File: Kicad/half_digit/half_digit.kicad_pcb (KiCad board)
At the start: 2 copper layers, 106.7 x 152.4 mm, 39 parts, among them J1 CONN_8, J2 CONN_8, J3 CONN_8, J4 CONN_8, J5 CONN_12, J6 CONN_12, J7 BARREL_JACK, U1 TLC5917, U2 AOZ1280, X1 MTHOLE, X2 MTHOLE, X3 MTHOLE, X4 MTHOLE

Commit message: Rough draft of half digit layout
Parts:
- added J8: CONN_12, HEADER_12X1, F.Cu at (135.3, 74.3)
- added J9: BARREL_JACK, PJ-036AH-SMT, F.Cu at (167.0, 205.7)
- J7: value BARREL_JACK -> CONN_12; footprint PJ-036AH-SMT -> HEADER_12X1
- moved J1 349.7 mm to (76.2, 205.7)
- moved J3 349.7 mm to (86.4, 205.7)
- moved R1 247.2 mm to (114.9, 130.2), turned to 90 degrees
- moved C4 236.8 mm to (119.4, 123.2), turned to 270 degrees
- moved C3 231.4 mm to (129.5, 195.6)
- moved D10 231.4 mm to (117.7, 144.8)
- moved D13 231.4 mm to (150.4, 144.8)
- moved D14 231.4 mm to (160.4, 144.8)
- moved D16 231.4 mm to (127.6, 200.0)
- moved D2 231.4 mm to (85.2, 113.9)
- moved D4 231.4 mm to (98.5, 190.8)
- moved D5 231.4 mm to (95.9, 176.0), turned to 180 degrees
- moved D6 231.4 mm to (93.3, 161.2)
- moved D7 231.4 mm to (137.3, 133.4), turned to 180 degrees
- moved D9 231.4 mm to (127.7, 144.8)
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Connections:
- J5 pad 12: (no net) -> N-0000031
- J5 pad 3: (no net) -> N-0000018
- J5 pad 4: (no net) -> N-0000017
- J5 pad 5: (no net) -> N-0000016
- J5 pad 6: (no net) -> N-0000019
- J6 pad 1: (no net) -> N-0000030
- J6 pad 10: (no net) -> N-0000023
- J6 pad 11: (no net) -> N-0000022
- J6 pad 2: (no net) -> N-0000029
- J6 pad 3: (no net) -> N-0000028
- J6 pad 4: (no net) -> N-0000027
- J6 pad 5: (no net) -> N-0000020
- J6 pad 6: (no net) -> N-0000026
- J6 pad 7: (no net) -> N-0000025
- J6 pad 8: (no net) -> N-0000024
- J7 pad 1: N-0000045 (its old number) -> +5V
- J7 pad 3: (no net) -> N-0000018
- PTC1 pad 1: N-0000045 (its old number) -> N-0000021
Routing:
- net GND: track 0.00 -> 472.2 mm, vias 0 -> 93
- net Vled: track 0.00 -> 384.6 mm, vias 0 -> 7
- net VCC: track 0.00 -> 294.2 mm, vias 0 -> 2
- net /LE: track 0.00 -> 276.7 mm, vias 0 -> 3
- net /CLK: track 0.00 -> 274.8 mm, vias 0 -> 3
- net /~OE: track 0.00 -> 266.4 mm, vias 0 -> 3
- net /SPARE: track 0.00 -> 238.4 mm, vias 0 -> 1
- net /SDO: track 0.00 -> 126.7 mm, vias 0 -> 1
- net +5V: track 0.00 -> 122.2 mm, vias 0 -> 2
- net N-000001: track 0.00 -> 101.4 mm, vias 0 -> 2
- net N-000008: track 0.00 -> 77.7 mm, vias 0 -> 2
- net N-000004: track 0.00 -> 73.6 mm, vias 0 -> 2
- net N-000005: track 0.00 -> 72.1 mm, vias 0 -> 2
- net N-0000010: track 0.00 -> 60.5 mm, vias 0 -> 2
- net N-000007: track 0.00 -> 48.0 mm
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- added copper zone on F.Cu, net +5V
- added copper zone on B.Cu, net GND
- added copper zone on F.Cu, net GND
- added copper zone on F.Cu, net N-0000026
- added copper zone on F.Cu, net N-0000036
- added copper zone on F.Cu, net Vled
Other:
- net class LED added: clearance 0.254, trace_width 0.635, via_dia 0.889, via_drill 0.635
- net class Power added: clearance 0.254, trace_width 1.27, via_dia 0.889, via_drill 0.635
- net class Superwide added: clearance 0.254, trace_width 2.54, via_dia 0.889, via_drill 0.635
- rule pad_to_mask_clearance: 0 -> 0.1778
- rule trace_min: 0.254 -> 0.127
- board text added: "1. All requests for design or material changes must be forwarded to Jason Cerundolo. No design or material changes shall be implemented without approval from Jason Cerundolo (jason@cerundolo.com)."
- board text added: "12V - 20V DC 5.5 mm OD 2.1 mm ID CTR POS"
- board text added: "2. Fabricate board using artwork. All typical dimensions are tolerance non-cumlative."
- board text added: "3. Acceptibility shall be based on IPC-A-600 Rev G. Performance must meet IPC-6012 Class 2."
- board text added: "4. MATERIAL: Laminated Glass Epoxy FR-4 or equivalent. Board thickness 0.062 inch. 1 oz Copper for all metal layers."
- board text added: "5. FABRICATION TOLERANCES: Trace/Space 8/8 mils. Trace width must maintain a +/- 20% in tolerance. All holes and registration must be within 0.008 inch of true position."
- board text added: "6. Hole sizes measured after plating."
- board text added: "7. FINAL PLATING: Hot Air Leveled Lead-free Solder."
- board text added: "8. Apply LPI soldermask both sides per IPC-SN-84D, Type A, Class 2, color - GREEN."
- board text added: "9. Screen print the legend on top side using non-conductive white epoxy ink. There should be no ink on pad, test point, or exposed metal as defined by solder mask layer."
- board text added: "A"
- board text added: "B"
- board text added: "C"
- board text added: "CLK"
- board text added: "Clock - Half Digit Rev 1 Reclaimer Labs 3 November 2014"
- board text added: "DP"
- board text added: "GND"
- board text added: "L"
- board text added: "LE"
- board text added: "NOTES (Unless otherwise specified.)"
- board text added: "R"
- board text added: "SPARE"
- board text added: "T"
- board text added: "VCC"
- board text added: "VLED"
- board text added: "~OE"

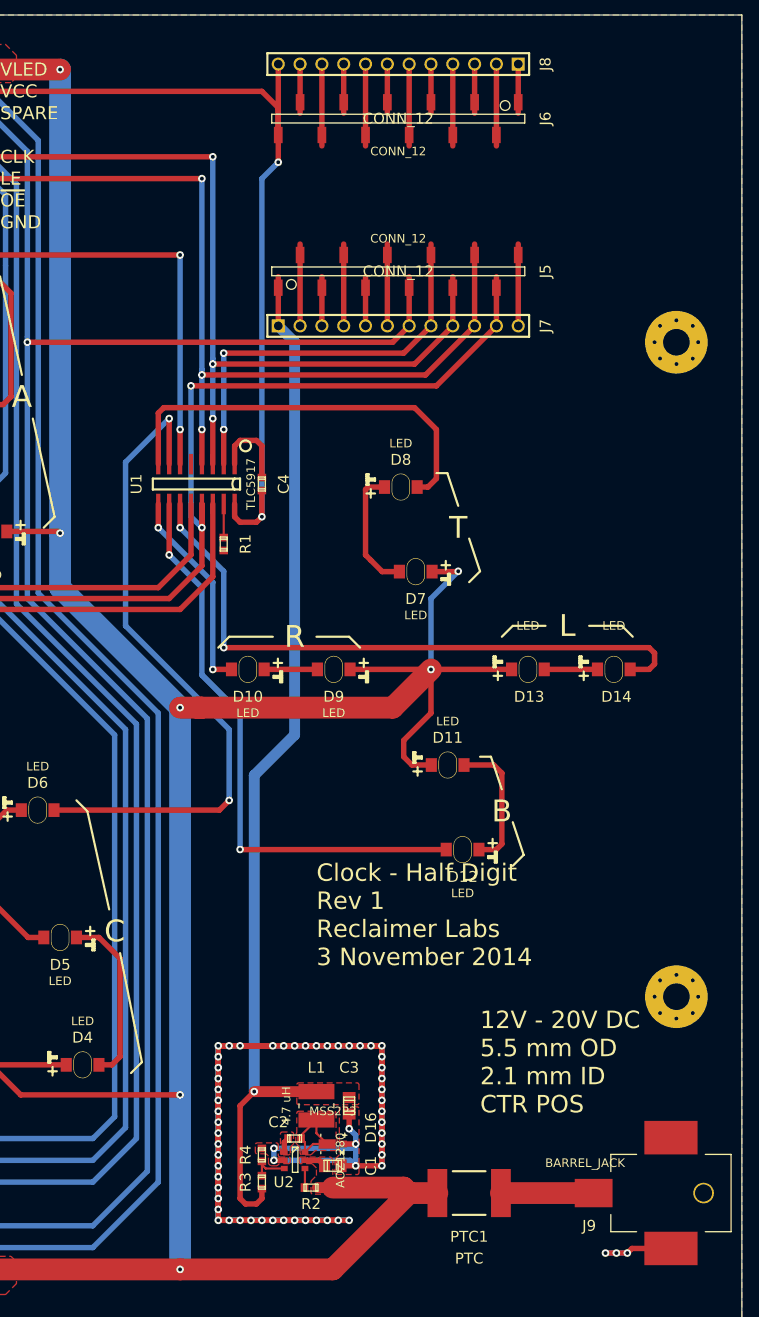
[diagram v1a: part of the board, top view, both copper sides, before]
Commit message: Initial Check-in of Enclosure
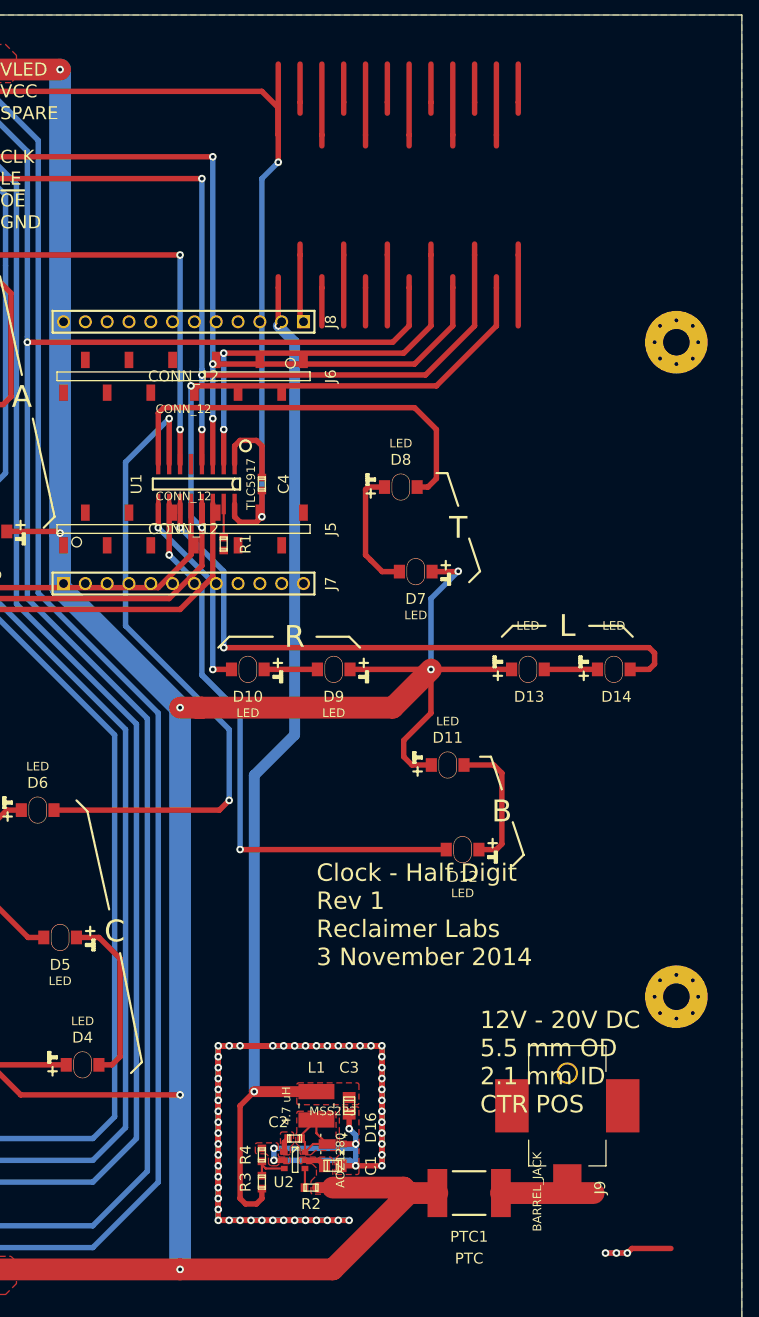
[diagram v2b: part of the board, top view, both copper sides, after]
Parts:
- moved J5 39.1 mm to (110.3, 128.4)
- moved J6 39.1 mm to (110.3, 110.6)
- moved J7 39.1 mm to (110.3, 134.8)
- moved J8 39.1 mm to (110.3, 104.3)
- moved J9 15.8 mm to (154.9, 195.6), turned to 270 degrees
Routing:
- net (no net): track 0.00 -> 121.9 mm
- net Vled: track 384.6 -> 310.9 mm, vias 7 -> 6
- net /~OE: track 266.4 -> 205.2 mm, vias 3 -> 2
- net N-0000026: track 9.52 -> 61.2 mm, vias 0 -> 1
- net N-0000029: track 9.52 -> 60.8 mm, vias 0 -> 1
- net VCC: track 294.2 -> 246.3 mm, vias 2 -> 0
- net /LE: track 276.7 -> 324.6 mm, vias 3 -> 5
- net /CLK: track 274.8 -> 232.3 mm, vias 3 -> 2
- net N-0000020: track 5.72 -> 42.5 mm, vias 0 -> 1
- net /SDI: track 47.9 -> 67.0 mm
- net N-000006: track 24.1 -> 4.94 mm
- net GND: track 472.2 -> 457.0 mm
- net +5V: track 122.2 -> 135.1 mm
- net N-0000031: track 9.53 -> 0.00 mm
- net N-0000019: track 9.53 -> 0.00 mm
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
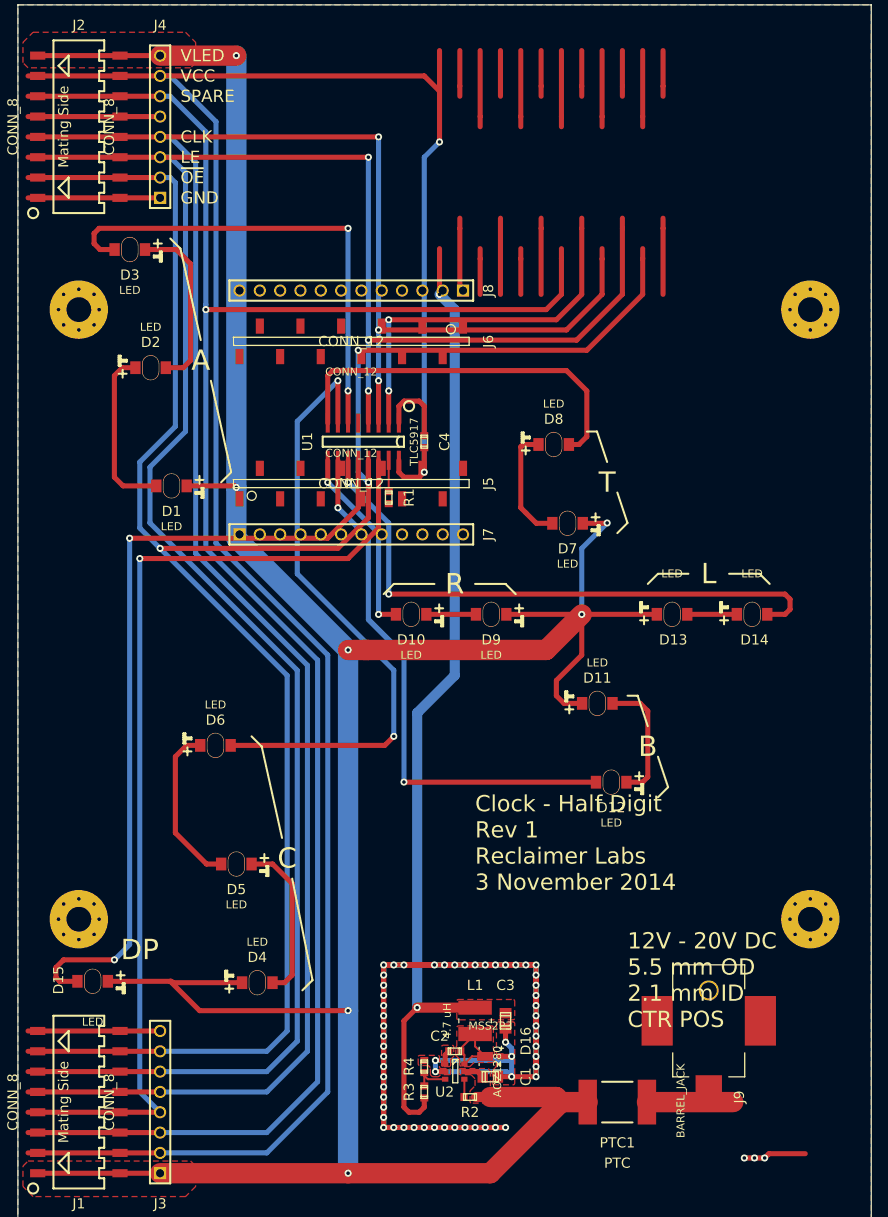
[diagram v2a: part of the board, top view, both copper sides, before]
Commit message: Half Digit Work
Moved spark landing pads to not interfere with L-bracket from OpenBeam
frame.
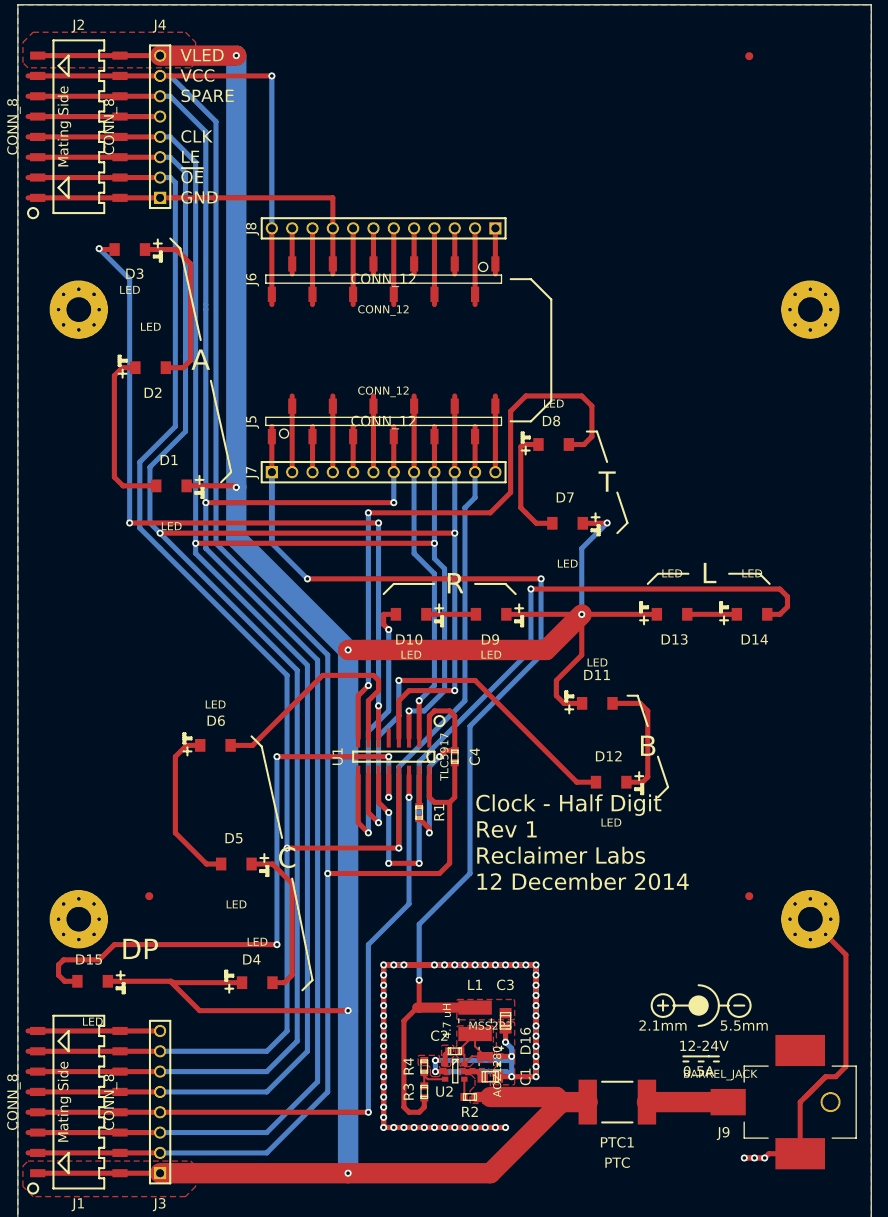
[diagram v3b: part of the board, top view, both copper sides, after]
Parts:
- added FIDUCIAL: VAL**, FIDUCIAL, F.Cu at (160.0, 75.0)
- added FIDUCIAL: VAL**, FIDUCIAL, F.Cu at (160.0, 180.0)
- added FIDUCIAL: VAL**, FIDUCIAL, F.Cu at (85.0, 180.0)
- moved C4 39.6 mm to (123.2, 162.6)
- moved U1 39.6 mm to (115.6, 162.6)
- moved R1 39.6 mm to (118.7, 169.5)
- moved J9 15.3 mm to (166.4, 205.7), turned to 180 degrees
- moved J5 8.76 mm to (114.3, 120.7)
- moved J7 8.76 mm to (114.3, 127.0)
- moved J8 8.76 mm to (114.3, 96.5)
- moved J6 8.76 mm to (114.3, 102.9)
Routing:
- net (no net): track 121.9 -> 0.00 mm
- net GND: track 457.0 -> 551.6 mm, vias 93 -> 95
- net Vled: track 310.9 -> 384.6 mm, vias 6 -> 7
- net /LE: track 324.6 -> 259.6 mm, vias 5 -> 3
- net N-0000026: track 61.2 -> 9.53 mm, vias 1 -> 0
- net N-0000029: track 60.8 -> 9.53 mm, vias 1 -> 0
- net N-000008: track 77.7 -> 30.1 mm, vias 2 -> 0
- net /~OE: track 205.2 -> 247.4 mm
- net /SDO: track 126.7 -> 86.8 mm, vias 1 -> 2
- net N-0000020: track 42.5 -> 5.72 mm, vias 1 -> 0
- net N-0000010: track 60.5 -> 95.8 mm, vias 2 -> 4
- net N-000006: track 4.94 -> 37.9 mm
- net N-000007: track 48.0 -> 76.2 mm, vias 0 -> 2
- net VCC: track 246.3 -> 270.5 mm, vias 0 -> 2
- net N-000001: track 101.4 -> 77.6 mm, vias 2 -> 4
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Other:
- net class Default: clearance 0.254 -> 0.2032
- net class LED: clearance 0.254 -> 0.2032
- rule trace_clearance: 0.254 -> 0.2032
- board text added: "0.5A"
- board text added: "12-24V"
- board text added: "2.1mm"
- board text added: "5.5mm"
- board text added: "Clock - Half Digit Rev 1 Reclaimer Labs 12 December 2014"
- board text removed: "12V - 20V DC 5.5 mm OD 2.1 mm ID CTR POS"
- board text removed: "Clock - Half Digit Rev 1 Reclaimer Labs 3 November 2014"
